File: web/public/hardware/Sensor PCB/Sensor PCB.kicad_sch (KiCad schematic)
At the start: 32 parts, among them J1 Conn_01x08_Pin, J2 Conn_01x08_Pin, J3 Conn_01x02_Pin, J4 Conn_01x02_Pin, U1 DRV5033FAQDBZR, U2 DRV5033FAQDBZR, U3 DRV5033FAQDBZR, U4 DRV5033FAQDBZR, U5 CD74HCT11, U6 CD74HCT11

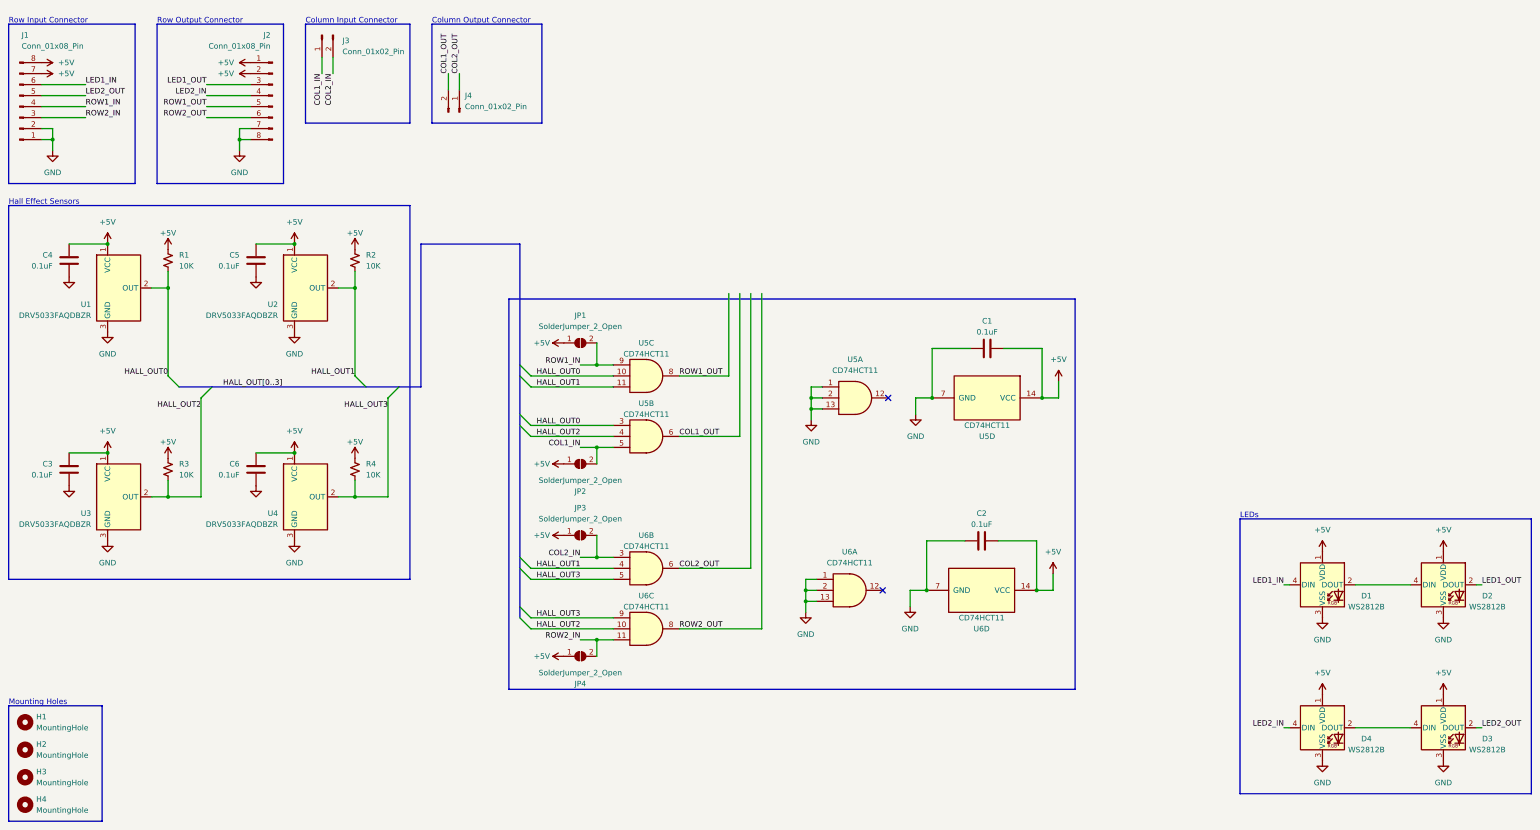
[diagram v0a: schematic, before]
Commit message: Complete layout without connectors wired
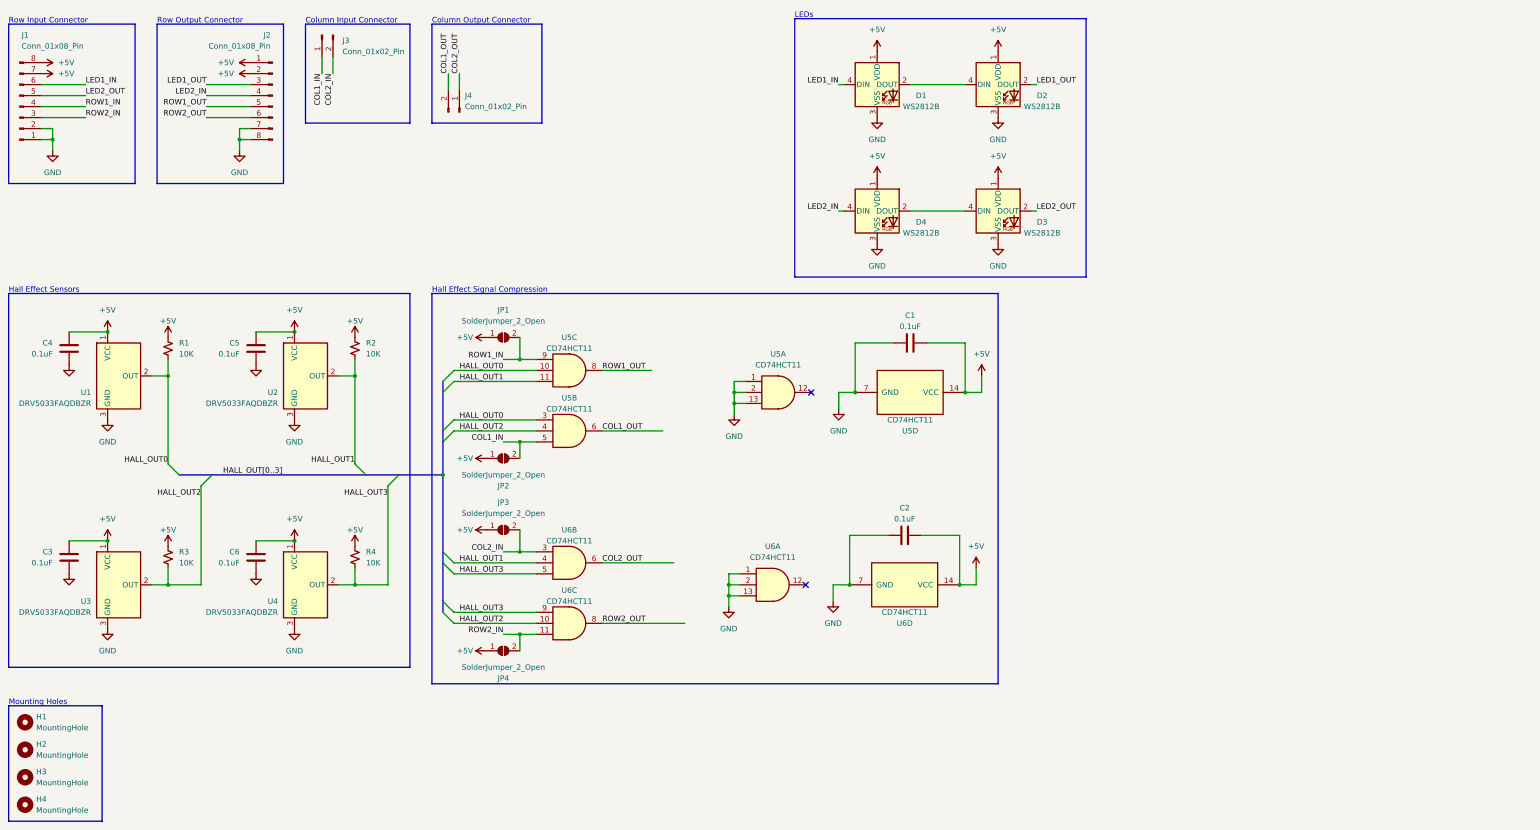
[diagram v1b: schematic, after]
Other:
- note added: "Hall Effect Signal Compression"
- moved on the sheet: C1, C2, C3, C4, C5, C6, D1, D2, D3, D4, JP1, JP2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
